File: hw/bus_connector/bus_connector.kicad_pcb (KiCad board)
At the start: 2 copper layers, 70 x 36 mm, 12 parts, among them J1 DE9_Left, J2 DE9_Top, J3 DE9_Right

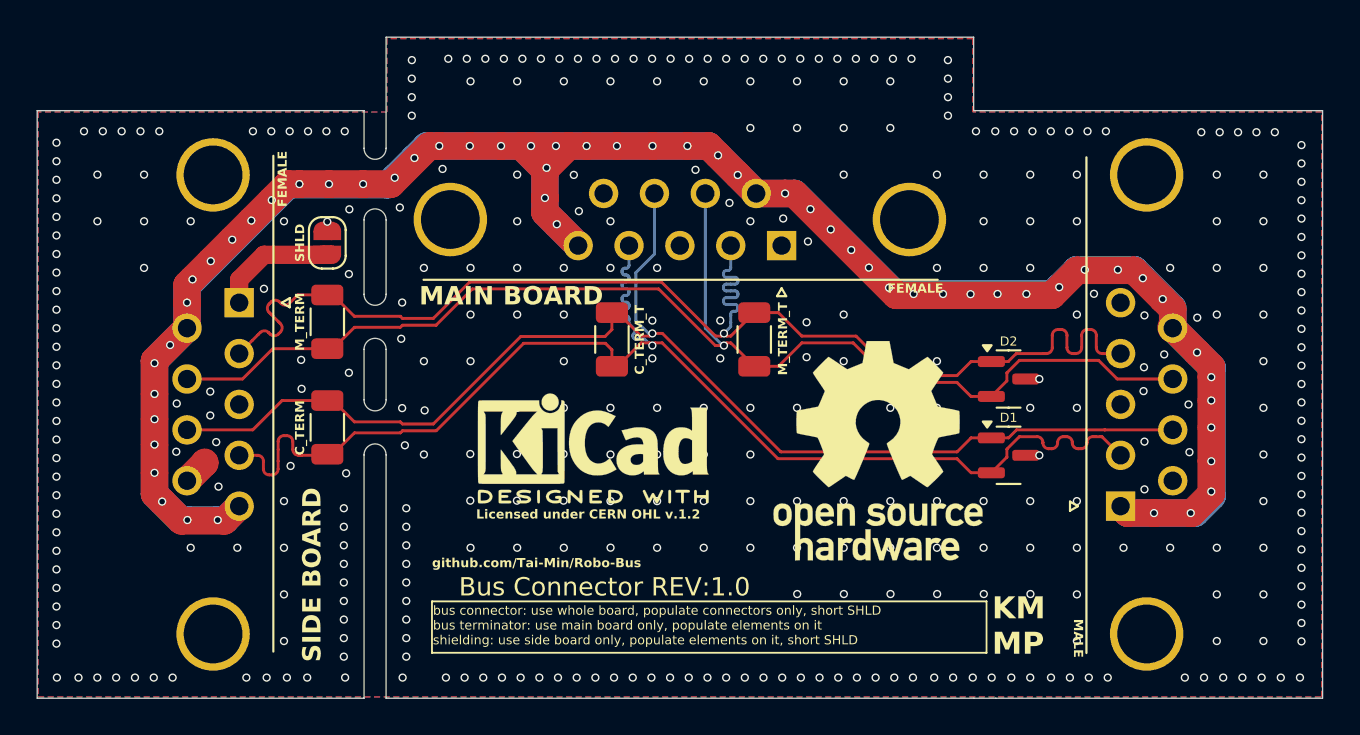
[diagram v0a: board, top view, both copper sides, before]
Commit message: Add QR code, remove shield jumper
Signed-off-by: Mateusz Pająk <22417805+Tai-Min@users.noreply.github.com>
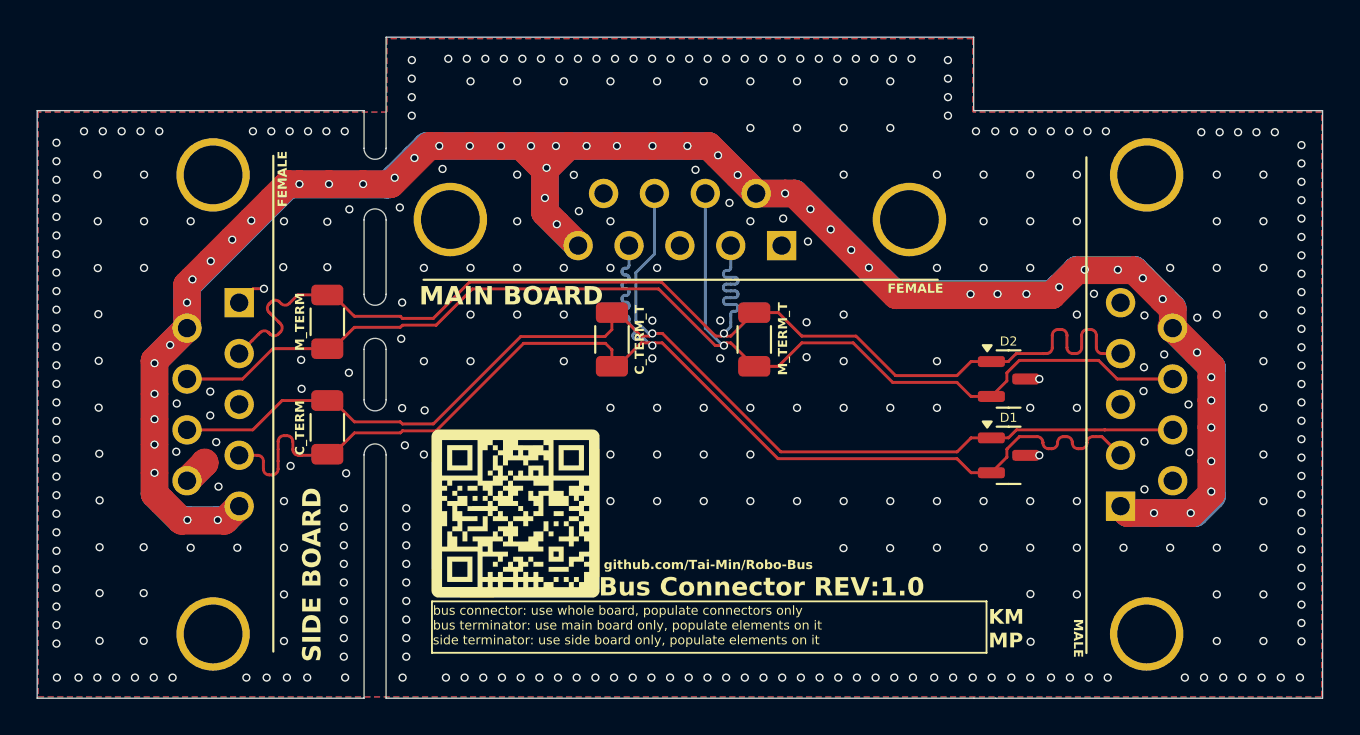
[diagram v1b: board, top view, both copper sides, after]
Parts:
- removed JP1: Shield_JMP, Jumper:SolderJumper-2_P1.3mm_Open_RoundedPad1.0x1.5mm
- added G***: LOGO, Logos:Robo-Bus, F.Cu at (137.6, 115.2)
- REF** (x2): moved to B.Cu
- moved REF** 16.2 mm to (141.1, 111.0), turned to 180 degrees
- moved REF** 14.8 mm to (156.6, 110.9), turned to 180 degrees
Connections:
- J1 pad 1: /SHIELD_L -> GND
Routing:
- net /SHIELD_L: track 6.62 -> 0.00 mm
- net GND: track 1.49 -> 3.16 mm, vias 369 -> 361
- net VCC: vias 58 -> 53
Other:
- board text added: "bus connector: use whole board, populate connectors only bus terminator: use main board only, populate elements on it side terminator: use side board only, populate elements on it"
- board text removed: "SHLD"
- board text removed: "bus connector: use whole board, populate connectors only, short SHLD bus terminator: use main board only, populate elements on it shielding: use side board only, populate elements on it, short SHLD"

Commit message: Add test points
Signed-off-by: Mateusz Pająk <22417805+Tai-Min@users.noreply.github.com>
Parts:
- removed the G*** at (137.6, 115.2)
- added G***: LOGO, symbols:robo-bus-qr, F.Cu at (137.5, 115.2)
- added TP1: TestPoint, TestPoint:TestPoint_Pad_D1.5mm, F.Cu at (140.3, 106.3)
- added TP2: TestPoint, TestPoint:TestPoint_Pad_D1.5mm, F.Cu at (140.3, 103.6)
- added TP3: TestPoint, TestPoint:TestPoint_Pad_D1.5mm, F.Cu at (161.3, 109.2)
- added TP4: TestPoint, TestPoint:TestPoint_Pad_D1.5mm, F.Cu at (161.3, 105.0)
- added TP5: TestPoint, TestPoint:TestPoint_Pad_D1.5mm, F.Cu at (166.8, 115.0)
- added TP6: TestPoint, TestPoint:TestPoint_Pad_D1.5mm, F.Cu at (149.2, 115.2)
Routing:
- net VCC: track 209.0 -> 213.1 mm, vias 53 -> 54
- net /MODBUS+: track 69.6 -> 72.6 mm
- net /MODBUS-: track 69.3 -> 72.2 mm
- net /CAN+: track 69.7 -> 72.2 mm
- net /CAN-: track 69.4 -> 71.8 mm
- net GND: vias 361 -> 371
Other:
- board text added: "CAN+"
- board text added: "CAN-"
- board text added: "GND"
- board text added: "RS485+"
- board text added: "RS485-"
- board text added: "VCC"

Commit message: Change versioning
Signed-off-by: Mateusz Pająk <22417805+Tai-Min@users.noreply.github.com>
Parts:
- moved REF** 8.08 mm to (153.4, 118.3)
- moved REF** 5.15 mm to (140.8, 116.1)
- moved G*** 3.19 mm to (137.3, 118.4)
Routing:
- net GND: vias 371 -> 384
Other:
- board text removed: "bus connector: use whole board, populate connectors only bus terminator: use main board only, populate elements on it side terminator: use side board only, populate elements on it"
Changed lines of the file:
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@@
 	(paper "A4")
 	(title_block
-		(title "Bus Connector")
+		(title "${TITLE}")
 		(date "2025-11-24")
-		(rev "1.0")
+		(rev "${REVISION}")
 	)
 	(layers
@@
 		)
 	)
+	(property "REVISION" "1.0.0d")
+	(property "TITLE" "Bus Connector")
 	(net 0 "")
 	(net 1 "VCC")
@@
 	(footprint "symbols:robo-bus-qr"
 		(layer "F.Cu")
-		(at 137.525001 115.184053)
+		(at 137.3124 118.364)
 		(property "Reference" "G***"
 			(at 0 0 0)
@@
 	(footprint "Symbol:KiCad-Logo2_5mm_SilkScreen"
 		(layer "B.Cu")
-		(at 156.609188 110.86 180)
+		(at 153.3652 118.2624 180)
 		(descr "KiCad Logo")
 		(tags "Logo KiCad")
@@
 	(footprint "Symbol:OSHW-Logo_11.4x12mm_SilkScreen"
 		(layer "B.Cu")
-		(at 141.109188 110.99 180)
+		(at 140.8176 116.1288 180)
 		(descr "Open Source Hardware Logo")
 		(tags "Logo OSHW")
@@
 		(layer "B.Mask")
 	)
-	(gr_rect
-		(start 133 119.2)
-		(end 163.2 122)
-		(stroke
-			(width 0.1)
-			(type default)
-		)
-		(fill no)
-		(layer "F.SilkS")
-	)
 	(gr_arc
 		(start 129.3 111.225)
@@
 	)
 	(gr_text "${TITLE} REV:${REVISION}"
-		(at 150.95 119 0)
+		(at 141.9352 122.174 0)
 		(layer "F.SilkS")
 		(effects
@@
 				(bold yes)
 			)
-			(justify bottom)
+			(justify left bottom)
 		)
 	)
@@
 	)
 	(gr_text "MAIN\nBOARD"
-		(at 142.175 116.675 0)
+		(at 141.962399 119.854947 0)
 		(layer "F.SilkS")
 		(effects
@@
 	)
 	(gr_text "github.com/Tai-Min/Robo-Bus"
-		(at 142.35 117.5 0)
+		(at 142.137399 120.679947 0)
 		(layer "F.SilkS")
 		(effects
@@
 		)
 	)
-	(gr_text "KM\nMP"
-		(at 163.3 121.8 0)
-		(layer "F.SilkS")
-		(effects
-			(font
-				(size 0.8 0.8)
-				(thickness 0.2)
-				(bold yes)
-			)
-			(justify left bottom)
-		)
-	)
 	(gr_text "FEMALE"
 		(at 125.15 97.725 90)
@@
 		)
 	)
-	(gr_text "bus connector: use whole board, populate connectors only\nbus terminator: use main board only, populate elements on it\nside terminator: use side board only, populate elements on it"
-		(at 133.05 121.6 0)
-		(layer "F.SilkS")
-		(effects
-			(font
-				(size 0.5 0.5)
-				(thickness 0.1)
-			)
-			(justify left bottom)
-		)
-	)
 	(gr_text "SIDE BOARD"
 		(at 127.05 117.75 -270)
@@
 		)
 	)
+	(gr_text "KM\nMP"
+		(at 134.4676 122.3264 -0)
+		(layer "B.SilkS")
+		(effects
+			(font
+				(size 0.8 0.8)
+				(thickness 0.2)
+				(bold yes)
+			)
+			(justify left bottom mirror)
+		)
+	)
 	(gr_text "Licensed under CERN OHL v.1.2"
-		(at 162.989188 114.75 0)
+		(at 159.7452 122.1524 0)
 		(layer "B.SilkS")
 		(effects
@@
 	)
 	(via
+		(at 152.8572 116.2812)
+		(size 0.45)
+		(drill 0.3)
+		(layers "F.Cu" "B.Cu")
+		(net 2)
+	)
+	(via
 		(at 124.94 118.82)
 		(size 0.45)
@@
 	)
 	(via
+		(at 152.8444 118.7516)
+		(size 0.45)
+		(drill 0.3)
+		(layers "F.Cu" "B.Cu")
+		(net 2)
+	)
+	(via
 		(at 165.58 116.28)
 		(size 0.45)
@@
 	)
 	(via
+		(at 135.128 111.2012)
+		(size 0.45)
+		(drill 0.3)
+		(layers "F.Cu" "B.Cu")
+		(net 2)
+	)
+	(via
 		(at 169.7 93.6)
 		(size 0.45)
@@
 	)
 	(via
+		(at 160.4872 118.7504)
+		(size 0.45)
+		(drill 0.3)
+		(layers "F.Cu" "B.Cu")
+		(net 2)
+	)
+	(via
 		(at 112.55 107.355172)
 		(size 0.45)
@@
 	)
 	(via
+		(at 157.9372 118.7704)
+		(size 0.45)
+		(drill 0.3)
+		(layers "F.Cu" "B.Cu")
+		(net 2)
+	)
+	(via
 		(at 180.35 116.373261)
 		(size 0.45)
@@
 	)
 	(via
+		(at 155.3972 118.7704)
+		(size 0.45)
+		(drill 0.3)
+		(layers "F.Cu" "B.Cu")
+		(net 2)
+	)
+	(via
 		(at 137.828512 123.35)
 		(size 0.45)
@@
 	)
 	(via
+		(at 147.7644 118.7516)
+		(size 0.45)
+		(drill 0.3)
+		(layers "F.Cu" "B.Cu")
+		(net 2)
+	)
+	(via
 		(at 147.35 95.7)
 		(size 0.45)
@@
 	)
 	(via
+		(at 137.668 111.2012)
+		(size 0.45)
+		(drill 0.3)
+		(layers "F.Cu" "B.Cu")
+		(net 2)
+	)
+	(via
+		(at 163.0272 118.7504)
+		(size 0.45)
+		(drill 0.3)
+		(layers "F.Cu" "B.Cu")
+		(net 2)
+	)
+	(via
 		(at 121.375 112.95)
 		(size 0.45)
@@
 	)
 	(via
+		(at 145.2372 116.2812)
+		(size 0.45)
+		(drill 0.3)
+		(layers "F.Cu" "B.Cu")
+		(net 2)
+	)
+	(via
 		(at 112.55 98.262069)
 		(size 0.45)
@@
 	)
 	(via
+		(at 140.208 111.2012)
+		(size 0.45)
+		(drill 0.3)
+		(layers "F.Cu" "B.Cu")
+		(net 2)
+	)
+	(via
 		(at 133.8878 89.65)
 		(size 0.45)
@@
 	)
 	(via
+		(at 142.6972 116.2812)
+		(size 0.45)
+		(drill 0.3)
+		(layers "F.Cu" "B.Cu")
+		(net 2)
+	)
+	(via
 		(at 124.94 98.5)
 		(size 0.45)
@@
 		(size 0.45)
 		(drill 0.3)
+		(layers "F.Cu" "B.Cu")
+		(net 2)
+	)
+	(via
+		(at 150.3172 118.7704)
+		(size 0.45)
+		(drill 0.3)

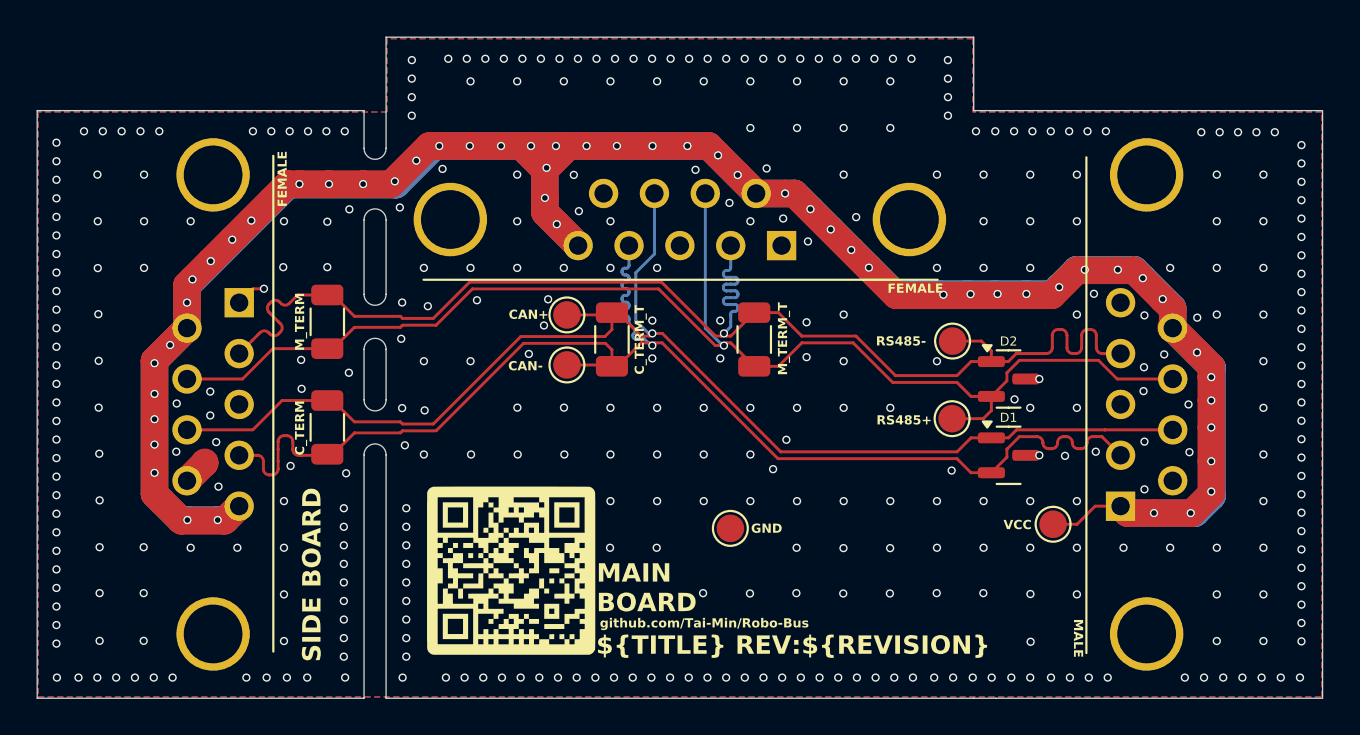
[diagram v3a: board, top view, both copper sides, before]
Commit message: Redo vias and VCC
Signed-off-by: Mateusz Pająk <22417805+Tai-Min@users.noreply.github.com>
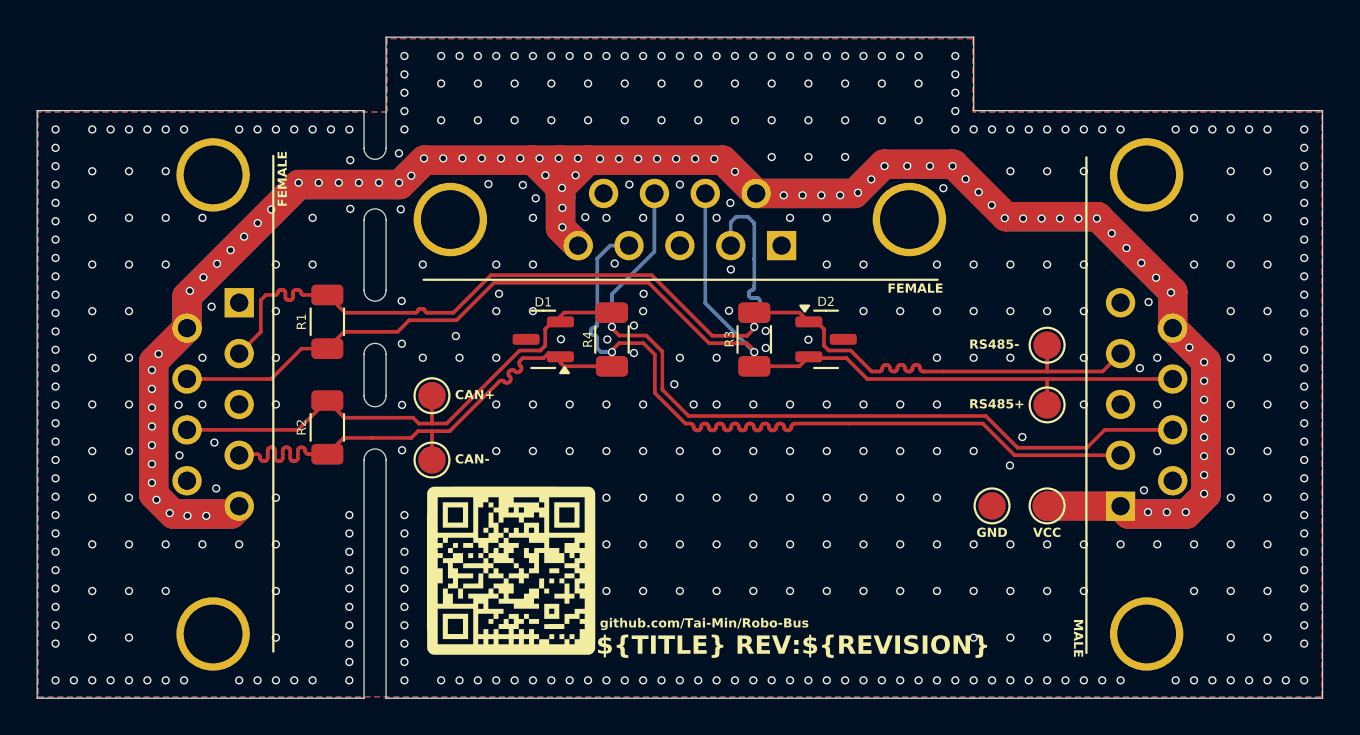
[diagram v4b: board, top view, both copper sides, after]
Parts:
- moved D1 26.1 mm to (139.1, 104.9), turned to 180 degrees
- moved TP6 14.3 mm to (163.5, 114.0)
- moved D2 10.2 mm to (154.5, 104.9)
- moved TP1 8.99 mm to (133.0, 111.5)
- moved TP2 8.57 mm to (133.0, 108.0)
- moved TP3 5.23 mm to (166.5, 108.5)
- moved TP4 5.15 mm to (166.5, 105.2)
- moved REF** 2.32 mm to (151.0, 118.3)
- moved REF** 2.32 mm to (138.5, 116.1)
- moved TP5 1.05 mm to (166.5, 114.0)
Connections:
- D1 pad 1: /CAN+ -> /CAN-
- D1 pad 2: /CAN- -> /CAN+
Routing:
- net GND: track 3.16 -> 0.09 mm, vias 384 -> 454
- net /MODBUS+: track 72.6 -> 70.1 mm
- net /MODBUS-: track 72.2 -> 70.0 mm
- net /CAN-: track 71.8 -> 72.8 mm
- net /CAN+: track 72.2 -> 73.0 mm
- net VCC: track 213.1 -> 213.5 mm, vias 54 -> 84
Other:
- outline, holes or cut-outs redrawn
- board text removed: "C_TERM"
- board text removed: "C_TERM_T"
- board text removed: "KM MP"
- board text removed: "MAIN BOARD"
- board text removed: "M_TERM"
- board text removed: "M_TERM_T"
- board text removed: "SIDE BOARD"
